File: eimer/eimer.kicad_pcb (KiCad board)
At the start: 2 copper layers, 72 x 72 mm, 71 parts, among them J3 Conn_01x03, J4 USB_C_Receptacle_USB2.0_14P, SW1 SW_Push, SW2 SW_Push, U1 RP2040, U2 MCP1700x-330xxTT, U3 TPS61221DCK, U4 W25Q16JVUXIQ TR, U5 LIS2DW12, Y1 12 MHz

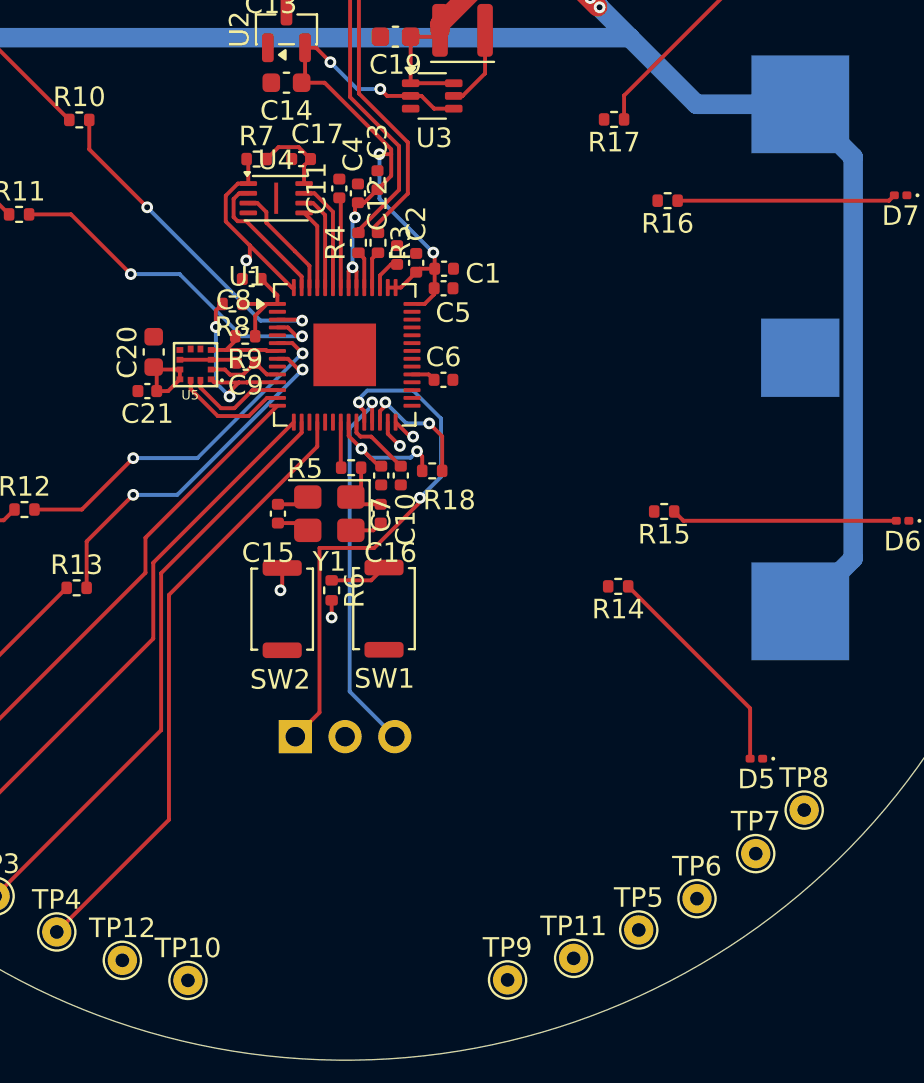
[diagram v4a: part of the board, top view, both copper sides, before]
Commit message: routed all gpios
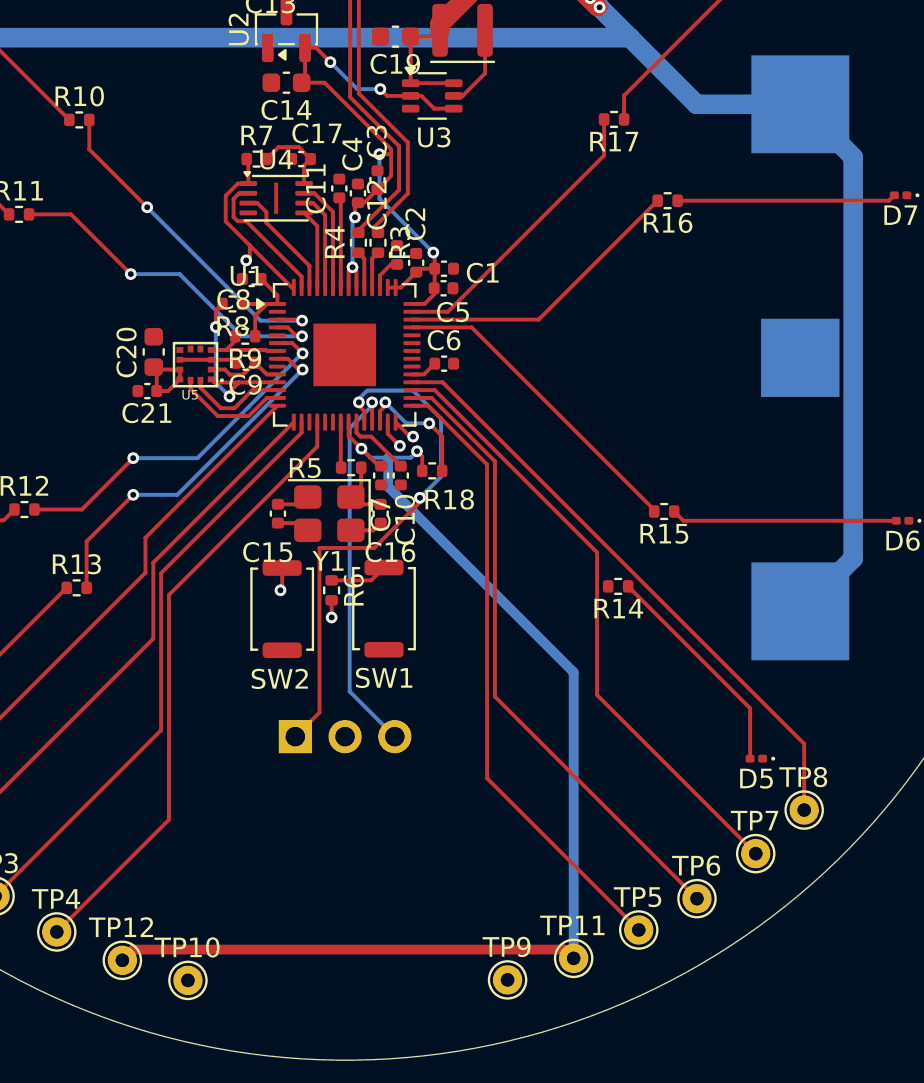
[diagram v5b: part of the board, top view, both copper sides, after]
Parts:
- moved C6 0.83 mm to (78.9, 89.5)
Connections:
- TP5 pad 1: unconnected-(TP5-Pad1) -> GPIO18
- TP6 pad 1: unconnected-(TP6-Pad1) -> GPIO19
- TP7 pad 1: unconnected-(TP7-Pad1) -> GPIO20
- TP8 pad 1: unconnected-(TP8-Pad1) -> GPIO21
- U1 pad 29: unconnected-(U1-GPIO18-Pad29) -> GPIO18
- U1 pad 30: unconnected-(U1-GPIO19-Pad30) -> GPIO19
- U1 pad 31: unconnected-(U1-GPIO20-Pad31) -> GPIO20
- U1 pad 32: unconnected-(U1-GPIO21-Pad32) -> GPIO21
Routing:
- net +3.3V: track 65.9 -> 119.0 mm
- net GPIO19: track 0.00 -> 32.2 mm
- net GPIO18: track 0.00 -> 32.1 mm
- net GPIO20: track 0.00 -> 31.6 mm
- net GPIO21: track 0.00 -> 31.1 mm
- net GPIO27/ADC1: track 0.00 -> 16.3 mm
- net GPIO28/ADC2: track 0.00 -> 15.1 mm
- net GPIO29/ADC3: track 0.00 -> 15.0 mm
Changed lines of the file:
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@@
 	(footprint "Capacitor_SMD:C_0402_1005Metric"
 		(layer "F.Cu")
-		(at 78.87 90.299888)
+		(at 78.905 89.475)
 		(descr "Capacitor SMD 0402 (1005 Metric), square (rectangular) end terminal, IPC-7351 nominal, (Body size source: IPC-SM-782 page 76, https://www.pcb-3d.com/wordpress/wp-content/uploads/ipc-sm-782a_amendment_1_and_2.pdf)")
 		(tags "capacitor")
@@
 			(layers "*.Cu" "*.Mask")
 			(remove_unused_layers no)
-			(net "unconnected-(TP6-Pad1)")
+			(net "GPIO19")
 			(pinfunction "1_1")
 			(pintype "passive")
@@
 			(layers "*.Cu" "*.Mask")
 			(remove_unused_layers no)
-			(net "unconnected-(TP7-Pad1)")
+			(net "GPIO20")
 			(pinfunction "1_1")
 			(pintype "passive")
@@
 			(layers "F.Cu" "F.Mask" "F.Paste")
 			(roundrect_rratio 0.25)
-			(net "unconnected-(U1-GPIO18-Pad29)")
+			(net "GPIO18")
 			(pinfunction "GPIO18_29")
 			(pintype "bidirectional")
@@
 			(layers "F.Cu" "F.Mask" "F.Paste")
 			(roundrect_rratio 0.25)
-			(net "unconnected-(U1-GPIO19-Pad30)")
+			(net "GPIO19")
 			(pinfunction "GPIO19_30")
-			(pintype "bidirectional+no_connect")
+			(pintype "bidirectional")
 		)
 		(pad "31" smd roundrect
@@
 			(layers "F.Cu" "F.Mask" "F.Paste")
 			(roundrect_rratio 0.25)
-			(net "unconnected-(U1-GPIO20-Pad31)")
+			(net "GPIO20")
 			(pinfunction "GPIO20_31")
 			(pintype "bidirectional")
@@
 			(layers "F.Cu" "F.Mask" "F.Paste")
 			(roundrect_rratio 0.25)
-			(net "unconnected-(U1-GPIO21-Pad32)")
+			(net "GPIO21")
 			(pinfunction "GPIO21_32")
-			(pintype "bidirectional+no_connect")
+			(pintype "bidirectional")
 		)
 		(pad "33" smd roundrect
@@
 			(net "unconnected-(U1-GPIO25-Pad37)")
 			(pinfunction "GPIO25_37")
-			(pintype "bidirectional+no_connect")
+			(pintype "bidirectional")
 		)
 		(pad "38" smd roundrect
@@
 			(layers "*.Cu" "*.Mask")
 			(remove_unused_layers no)
-			(net "unconnected-(TP5-Pad1)")
+			(net "GPIO18")
 			(pinfunction "1_1")
 			(pintype "passive")
@@
 			(layers "*.Cu" "*.Mask")
 			(remove_unused_layers no)
-			(net "unconnected-(TP8-Pad1)")
+			(net "GPIO21")
 			(pinfunction "1_1")
 			(pintype "passive")
@@
 	)
 	(segment
-		(start 77.263961 90.024888)
-		(end 78.115 90.024888)
+		(start 78.395 76.45)
+		(end 77.745 75.8)
 		(width 0.2)
 		(layer "F.Cu")
@@
 	)
 	(segment
-		(start 78.395 76.45)
-		(end 77.745 75.8)
+		(start 71.471461 78.414888)
+		(end 72.081461 79.024888)
 		(width 0.2)
 		(layer "F.Cu")
@@
 	)
 	(segment
-		(start 71.471461 78.414888)
-		(end 72.081461 79.024888)
+		(start 77.875112 90.024888)
+		(end 78.425 89.475)
 		(width 0.2)
 		(layer "F.Cu")
@@
 	)
 	(segment
+		(start 63.02 119.4)
+		(end 62.47 119.95)
+		(width 0.5)
+		(layer "F.Cu")
+		(net "+3.3V")
+	)
+	(segment
 		(start 70.388849 86.425)
 		(end 70.388961 86.424888)
@@
 	)
 	(segment
+		(start 85.52 119.85)
+		(end 85.07 119.4)
+		(width 0.5)
+		(layer "F.Cu")
+		(net "+3.3V")
+	)
+	(segment
 		(start 78.421461 85.599888)
 		(end 78.396461 85.624888)
@@
 	)
 	(segment
+		(start 77.263961 90.024888)
+		(end 77.875112 90.024888)
+		(width 0.2)
+		(layer "F.Cu")
+		(net "+3.3V")
+	)
+	(segment
 		(start 69.25 89.425)
 		(end 69.849888 90.024888)
@@
 	)
 	(segment
+		(start 85.07 119.4)
+		(end 63.02 119.4)
+		(width 0.5)
+		(layer "F.Cu")
+		(net "+3.3V")
+	)
+	(segment
 		(start 75.601461 78.774888)
 		(end 76.201461 78.774888)
@@
 	)
 	(segment
-		(start 78.115 90.024888)
-		(end 78.39 90.299888)
-		(width 0.2)
-		(layer "F.Cu")
-		(net "+3.3V")
-	)
-	(segment
 		(start 67.963866 90.035)
 		(end 68.64 90.035)
@@
 	)
 	(segment
+		(start 76.05 95.765661)
+		(end 85.52 105.235661)
+		(width 0.5)
+		(layer "B.Cu")
+		(net "+3.3V")
+	)
+	(segment
 		(start 75.601461 81.049888)
 		(end 75.601461 78.774888)
@@
 	)
 	(segment
+		(start 76.05 94.275)
+		(end 76.05 95.765661)
+		(width 0.5)
+		(layer "B.Cu")
+		(net "+3.3V")
+	)
+	(segment
+		(start 85.52 105.235661)
+		(end 85.52 119.85)
+		(width 0.5)
+		(layer "B.Cu")
+		(net "+3.3V")
+	)
+	(segment
 		(start 78.351461 83.799888)
 		(end 75.601461 81.049888)
@@
 	(segment
 		(start 75.139526 94.275)
+		(end 76.05 94.275)
+		(width 0.2)
+		(layer "B.Cu")
+		(net "+3.3V")
+	)
+	(segment
+		(start 76.05 94.275)
 		(end 77.195 94.275)
 		(width 0.2)
@@
 	)
 	(segment
+		(start 87.075 78.842483)
+		(end 87.075 77)
+		(width 0.2)
+		(layer "F.Cu")
+		(net "GPIO29{slash}ADC3")
+	)
+	(segment
+		(start 77.263961 86.824888)
+		(end 79.092595 86.824888)
+		(width 0.2)
+		(layer "F.Cu")
+		(net "GPIO29{slash}ADC3")
+	)
+	(segment
+		(start 79.092595 86.824888)
+		(end 87.075 78.842483)
+		(width 0.2)
+		(layer "F.Cu")
+		(net "GPIO29{slash}ADC3")
+	)
+	(segment
 		(start 67.245 86.765)
 		(end 67.585 86.425)
@@
 	)
 	(segment
+		(start 77.263961 87.624888)
+		(end 80.315964 87.624888)
+		(width 0.2)
+		(layer "F.Cu")
+		(net "GPIO27{slash}ADC1")
+	)
+	(segment
+		(start 89.635 96.943924)
+		(end 89.635 97.025)
+		(width 0.2)
+		(layer "F.Cu")
+		(net "GPIO27{slash}ADC1")
+	)
+	(segment
+		(start 80.315964 87.624888)
+		(end 89.635 96.943924)
+		(width 0.2)
+		(layer "F.Cu")
+		(net "GPIO27{slash}ADC1")
+	)
+	(segment
+		(start 83.735112 87.224888)
+		(end 89.81 81.15)
+		(width 0.2)
+		(layer "F.Cu")
+		(net "GPIO28{slash}ADC2")
+	)
+	(segment
+		(start 77.263961 87.224888)
+		(end 83.735112 87.224888)
+		(width 0.2)
+		(layer "F.Cu")
+		(net "GPIO28{slash}ADC2")
+	)
+	(segment
 		(start 72.101461 67.594888)
 		(end 72.076461 67.569888)
@@
 		(net "GPIO15")
 	)
+	(segment
+		(start 78.093417 91.624888)
+		(end 77.263961 91.624888)
+		(width 0.2)
+		(layer "F.Cu")
+		(net "GPIO18")
+	)
+	(segment
+		(start 81.1 94.631471)
+		(end 78.093417 91.624888)
+		(width 0.2)
+		(layer "F.Cu")
+		(net "GPIO18")
+	)
+	(segment
+		(start 88.845 118.4)
+		(end 81.1 110.655)
+		(width 0.2)
+		(layer "F.Cu")
+		(net "GPIO18")
+	)
+	(segment
+		(start 81.1 110.655)
+		(end 81.1 94.631471)
+		(width 0.2)
+		(layer "F.Cu")
+		(net "GPIO18")
+	)
+	(segment
+		(start 81.5 94.465786)
+		(end 78.259102 91.224888)
+		(width 0.2)
+		(layer "F.Cu")
+		(net "GPIO19")
+	)
+	(segment
+		(start 91.82 116.8)
+		(end 81.5 106.48)
+		(width 0.2)
+		(layer "F.Cu")
+		(net "GPIO19")
+	)
+	(segment
+		(start 81.5 106.48)
+		(end 81.5 94.465786)
+		(width 0.2)
+		(layer "F.Cu")
+		(net "GPIO19")
+	)
+	(segment
+		(start 78.259102 91.224888)
+		(end 77.263961 91.224888)
+		(width 0.2)
+		(layer "F.Cu")
+		(net "GPIO19")
+	)
+	(segment
+		(start 78.424788 90.824888)
+		(end 77.263961 90.824888)
+		(width 0.2)
+		(layer "F.Cu")
+		(net "GPIO20")
+	)
+	(segment
+		(start 94.82 114.5)
+		(end 86.715 106.395)
+		(width 0.2)
+		(layer "F.Cu")
+		(net "GPIO20")
+	)
+	(segment
+		(start 86.715 99.1151)
+		(end 78.424788 90.824888)
+		(width 0.2)
+		(layer "F.Cu")
+		(net "GPIO20")
+	)
+	(segment
+		(start 86.715 106.395)
+		(end 86.715 99.1151)
+		(width 0.2)
+		(layer "F.Cu")
+		(net "GPIO20")
+	)
+	(segment
+		(start 97.295 108.895)
+		(end 78.824888 90.424888)
+		(width 0.2)
+		(layer "F.Cu")
+		(net "GPIO21")
+	)
+	(segment
+		(start 78.824888 90.424888)
+		(end 77.263961 90.424888)
+		(width 0.2)
+		(layer "F.Cu")
+		(net "GPIO21")
+	)
+	(segment
+		(start 97.295 112.275)
+		(end 97.295 108.895)
+		(width 0.2)
+		(layer "F.Cu")
+		(net "GPIO21")
+	)
 	(embedded_fonts no)

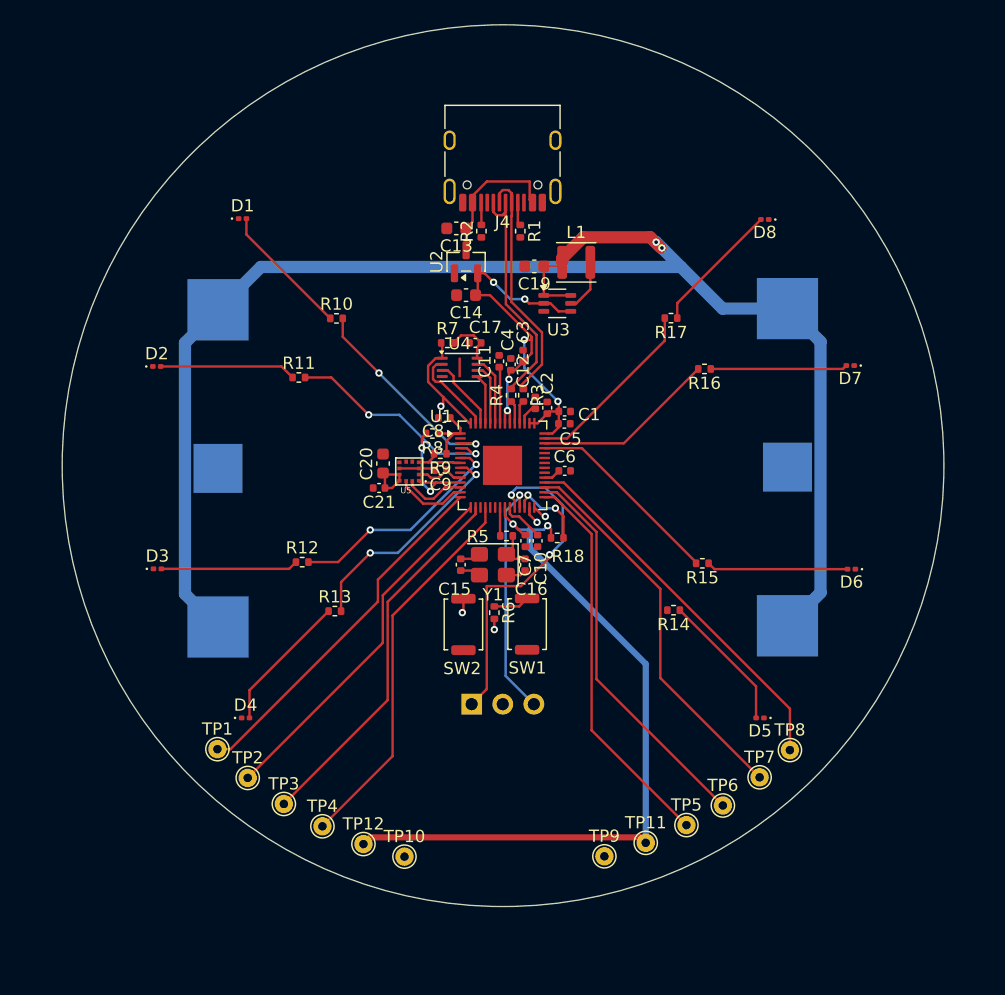
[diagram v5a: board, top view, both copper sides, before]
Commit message: poured ground plane
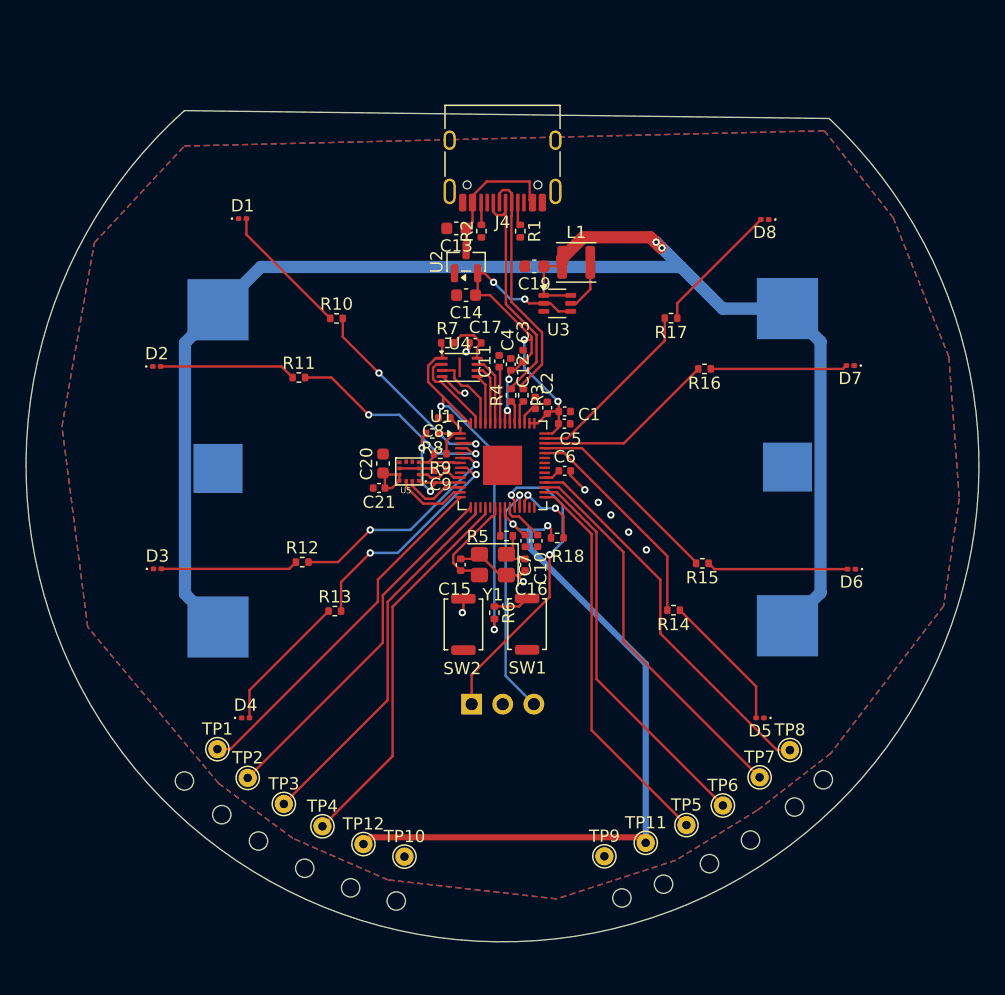
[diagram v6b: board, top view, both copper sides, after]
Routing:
- net QSPI_SS: track 10.6 -> 31.0 mm
- net GPIO26/ADC0: track 0.00 -> 17.9 mm
- net GND: track 6.30 -> 15.2 mm, vias 0 -> 8
- net XIN: track 1.68 -> 8.56 mm
- net SWCLK: track 27.2 -> 25.6 mm
- net unconnected-(U1-GPIO16-Pad27): track 1.47 -> 0.00 mm, vias 1 -> 0
- net unconnected-(U1-GPIO17-Pad28): track 1.20 -> 0.00 mm, vias 1 -> 0
- net QSPI_SD2: track 5.88 -> 6.48 mm
- net GPIO21: track 31.1 -> 31.7 mm
- added copper zone on B.Cu, net GND
- added copper zone on F.Cu, net GND
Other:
- board size 72 x 72 mm -> 77.8 x 67.9 mm

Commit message: finished all routing
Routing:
- net Net-(U1-RUN): track 7.69 -> 25.3 mm, vias 3 -> 4
- net +3.3V: track 119.0 -> 124.3 mm
- net GND: track 15.2 -> 19.1 mm
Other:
- board size 77.8 x 67.9 mm -> 78 x 68.1 mm
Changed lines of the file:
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@@
 		(layer "Edge.Cuts")
 	)
-	(gr_circle
-		(center 100.025 114.7)
-		(end 100.775 114.7)
+	(gr_arc
+		(start 100 60.1)
+		(mid 73.738464 128.034983)
+		(end 47.778586 59.984157)
 		(stroke
 			(width 0.05)
-			(type solid)
+			(type default)
 		)
-		(fill no)
 		(layer "Edge.Cuts")
 	)
 	(gr_line
-		(start 100.5 60.700002)
+		(start 100 60.1)
 		(end 47.8465 60.059871)
 		(stroke
@@
 		(layer "Edge.Cuts")
 	)
-	(gr_arc
-		(start 100.5 60.7)
-		(mid 73.352011 127.930495)
-		(end 47.846498 60.059871)
+	(gr_circle
+		(center 100.025 114.7)
+		(end 100.775 114.7)
 		(stroke
 			(width 0.05)
-			(type default)
+			(type solid)
 		)
+		(fill no)
 		(layer "Edge.Cuts")
 	)
@@
 	)
 	(segment
+		(start 72.826461 90.024888)
+		(end 73.826461 89.024888)
+		(width 0.2)
+		(layer "F.Cu")
+		(net "GND")
+	)
+	(segment
 		(start 74.14 97.9875)
 		(end 73.64 97.9875)
@@
 	)
 	(segment
+		(start 72.826461 92.462388)
+		(end 72.826461 90.024888)
+		(width 0.2)
+		(layer "F.Cu")
+		(net "GND")
+	)
+	(segment
 		(start 75.525 98.525)
 		(end 75.025 98.025)
@@
 	)
 	(segment
-		(start 76.201461 78.526359)
+		(start 74.312551 76.637449)
 		(end 72.79999 75.124888)
 		(width 0.2)
@@
 	)
 	(segment
+		(start 65.4075 89.775)
+		(end 67.0075 89.775)
+		(width 0.2)
+		(layer "F.Cu")
+		(net "+3.3V")
+	)
+	(segment
 		(start 76.426461 85.587388)
 		(end 76.693961 85.587388)
@@
 	)
 	(segment
+		(start 71.3 78.414888)
+		(end 72.535112 78.414888)
+		(width 0.2)
+		(layer "F.Cu")
+		(net "+3.3V")
+	)
+	(segment
 		(start 78.396461 85.624888)
 		(end 78.396461 85.934887)
@@
 	)
 	(segment
+		(start 70.446461 78.414888)
+		(end 71.3 78.414888)
+		(width 0.2)
+		(layer "F.Cu")
+		(net "+3.3V")
+	)
+	(segment
 		(start 74.426461 84.749888)
 		(end 74.226461 84.549888)
@@
 	)
 	(segment
+		(start 76.201461 78.526359)
+		(end 74.312551 76.637449)
+		(width 0.2)
+		(layer "F.Cu")
+		(net "+3.3V")
+	)
+	(segment
 		(start 77.195 75.8)
 		(end 75.995 75.8)
@@
 	)
 	(segment
+		(start 72.535112 78.414888)
+		(end 74.312551 76.637449)
+		(width 0.2)
+		(layer "F.Cu")
+		(net "+3.3V")
+	)
+	(segment
 		(start 74.026461 84.749888)
 		(end 74.226461 84.549888)
@@
 	)
 	(segment
-		(start 70.446461 78.414888)
+		(start 71.3 78.414888)
 		(end 71.471461 78.414888)
 		(width 0.2)
@@
 	)
 	(segment
-		(start 70.633539 100.961461)
-		(end 70.545 101.05)
+		(start 78.805 94.95)
+		(end 78.805 99.194485)
 		(width 0.2)
 		(layer "F.Cu")
@@
 	)
 	(segment
+		(start 75.626461 91.898417)
+		(end 75.901461 91.623417)
+		(width 0.2)
+		(layer "F.Cu")
+		(net "Net-(U1-RUN)")
+	)
+	(segment
+		(start 70.633539 101.408539)
+		(end 72.9 103.675)
+		(width 0.2)
+		(layer "F.Cu")
+		(net "Net-(U1-RUN)")
+	)
+	(segment
 		(start 70.633539 99.912612)
-		(end 70.633539 100.961461)
+		(end 70.633539 101.408539)
 		(width 0.2)
 		(layer "F.Cu")
@@
 	)
 	(segment
-		(start 75.626461 91.898417)
-		(end 75.901461 91.623417)
+		(start 73.225 104.774485)
+		(end 73.225 105.15)
 		(width 0.2)
 		(layer "F.Cu")
@@
 		(net "Net-(U1-RUN)")
 	)
+	(segment
+		(start 78.805 99.194485)
+		(end 73.225 104.774485)
+		(width 0.2)
+		(layer "F.Cu")
+		(net "Net-(U1-RUN)")
+	)
 	(via
 		(at 75.901461 91.449888)
@@
 	)
 	(via
-		(at 70.545 101.05)
+		(at 72.9 103.675)
 		(size 0.6)
 		(drill 0.3)
 		(layers "F.Cu" "B.Cu")
-		(free yes)
 		(net "Net-(U1-RUN)")
 	)
@@
 		(net "Net-(U1-RUN)")
 	)
+	(via
+		(at 73.225 105.15)
+		(size 0.6)
+		(drill 0.3)
+		(layers "F.Cu" "B.Cu")
+		(net "Net-(U1-RUN)")
+	)
+	(segment
+		(start 73.225 104)
+		(end 72.9 103.675)
+		(width 0.2)
+		(layer "B.Cu")
+		(net "Net-(U1-RUN)")
+	)
+	(segment
+		(start 73.225 105.15)
+		(end 73.225 104)
+		(width 0.2)
+		(layer "B.Cu")
+		(net "Net-(U1-RUN)")
+	)
 	(segment
 		(start 76.976573 92.525)
@@
 		(polygon
 			(pts
-				(xy 100.1 61.7) (xy 105.725 68.8) (xy 110.275 80.175) (xy 111.125 91.725) (xy 109.85 100.5) (xy 100.625 112.55)
+				(xy 99.875 61.15) (xy 105.725 68.8) (xy 110.275 80.175) (xy 111.125 91.725) (xy 109.85 100.5) (xy 100.625 112.55)
 				(xy 94.625 117.2) (xy 87.975 121.275) (xy 78.25 124.425) (xy 64.475 122.875) (xy 56.7 119.475) (xy 50.65 115)
-				(xy 39.95 102.225) (xy 37.85 85.85) (xy 40.5 70.85) (xy 47.85 62.95)
+				(xy 39.95 102.225) (xy 37.85 85.85) (xy 40.5 70.85) (xy 48.325 61.225)
 			)
 		)

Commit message: removed some silkscreen text
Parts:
- renumbered TP12 to 3.3V, TP11 to 3.3V, TP9 to GND, TP10 to GND, TP1 to GPIO11, TP2 to GPIO12, TP3 to GPIO13, TP4 to GPIO15, TP5 to GPIO18, TP6 to GPIO19, TP7 to GPIO20, TP8 to GPIO21, SW2 to reset, SW1 to run
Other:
- outline, holes or cut-outs redrawn
